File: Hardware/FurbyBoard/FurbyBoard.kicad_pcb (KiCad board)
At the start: 4 copper layers, 68.8 x 74.6 mm, 155 parts, among them J1 USB-C 16P, J11 J_EXP: header de expansión si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, J2 BAT+, J3 BAT-, J5 Micro I2S (3V3, GND, SCK, WS,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, J6 FPC 24P 0.5, J7 Frente: IR (emisor ×2, recept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, J8 Inclinación ×3, lengua ×2, al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, J9 Leva ×2, encoder ×4, barriga 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, Q1 SI7615ADN, Q2 AO3400A, Q3 AO3400A, SW1 RESET, SW2 BOOT, U1 USBLC6-2SC6, U10 TCA9535PWR, U11 SN74LVC1G17DBVR, U2 BQ24073RGTR, U3 TPS63802DLAR, U4 ESP32-S3-WROOM-1-N16R8, U5 TPS61089RNRR, U6 DRV8231ADSGR, U7 MAX98357AETE+T, U8 ME6211C28M5G-N, U9 ME6211C12M5G-N

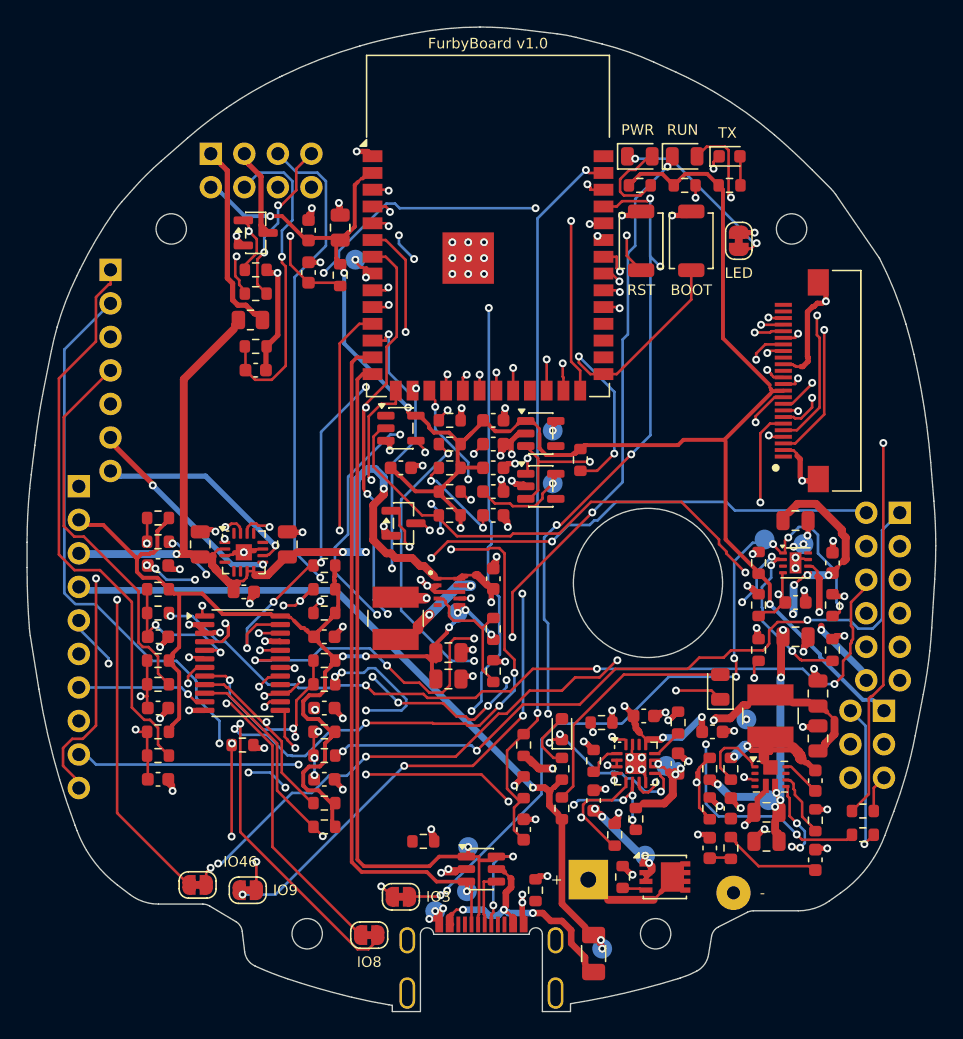
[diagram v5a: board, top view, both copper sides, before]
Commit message: Feature: replanteo de la planta y colocación de la FurbyBoard (puerta C, sin rutar)
- Partición nueva: motor y elevador en la esquina trasera derecha junto a J9, cargador en el centro trasero con los pads de batería, LDO de cámara bajo el FPC, expansor pegado a la columna izquierda del módulo, amplificador junto a J8, buck-boost en la zona trasera izquierda; J8, J5 y J_EXP en el borde izquierdo; TP en la cara inferior junto a su fuente.
- Pasillos reservados: cámara (módulo -> J6), sur, canal de la columna izquierda y norte-sur (par USB).
- gen_pcb.py: cara por pieza, keepout de cobre de las cabezas de tornillo, franja del flex sin piezas, logo recolocado; comprobar_colocacion.py vigila el flex y los TP de la cara inferior.
- Puerta C: DRC 0/0 con paridad (362 conexiones sin rutar, esperable), comprobar-flujo PASS (0 errores, 4 avisos de desacoplo a 1-1,9 mm), 12 PNG revisados. Informe en revisiones/ y NOTAS.md reescrito con la plantilla.

Co-Authored-By: Claude Fable 5.1 <noreply@anthropic.com>
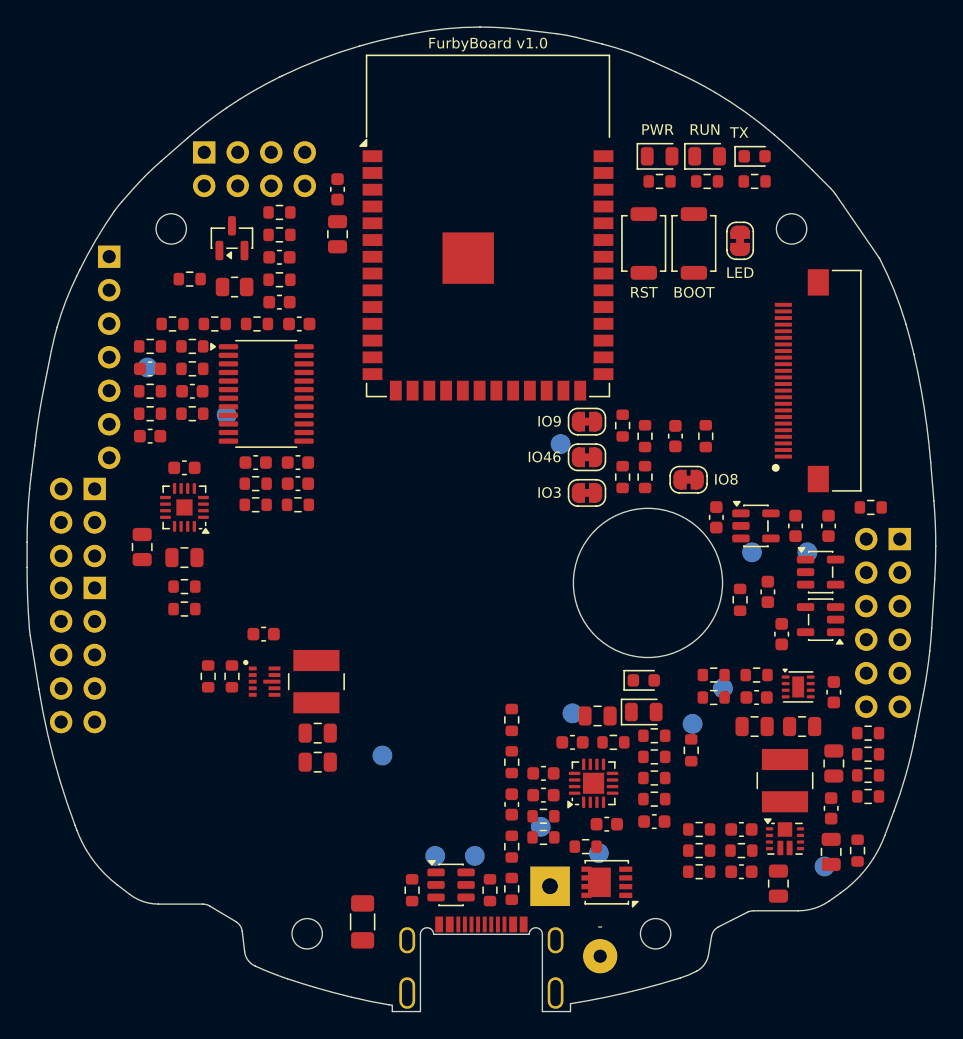
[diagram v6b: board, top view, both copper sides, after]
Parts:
- removed Q2: AO3400A, Package_TO_SOT_SMD:SOT-23
- J11: value J_EXP: header de expansión sin montar -> J_EXP: header de expansión 2 x 5 sin montar; footprint FurbyBoard:Pads_1x10_P2.54mm -> FurbyBoard:Pads_2x05_P2.54mm
- J5: value Micro I2S (3V3, GND, SCK, WS, SD, L/R) -> Micro I2S (SD, GND, SCK, WS, 3V3, GND)
- J9: value Leva ×2, encoder ×4, barriga ×2, espalda ×2, motor ×2 -> Encoder ×3, leva ×2, barriga ×2, espalda ×2, motor ×2 (más GND)
- R51: value 220 -> 470
- moved J5 62.1 mm to (117.2, 48.2)
- moved R40 55.7 mm to (175.8, 66.7)
- moved R42 54.9 mm to (175.8, 68.3)
- moved R32 54.2 mm to (124.0, 57.3)
- moved R31 54.1 mm to (124.0, 55.6)
- moved TP14 51.5 mm to (121.2, 39.0), turned to 0 degrees
- moved JP1 43.8 mm to (154.5, 43.1)
- moved JP2 43.8 mm to (154.5, 45.8)
- moved JP4 42.1 mm to (162.2, 47.5)
- moved R50 41.2 mm to (175.8, 69.9)
- moved R51 39.2 mm to (175.8, 71.5)
- moved TP12 36.6 mm to (152.5, 44.8), turned to 0 degrees
- moved U11 34.9 mm to (172.2, 58.1), turned to 180 degrees
- moved R25 34.0 mm to (162.4, 68.0), turned to 90 degrees
- moved JP3 33.7 mm to (154.5, 48.5)
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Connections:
- net BB_L1 renamed BB_SW1
- net BB_L2 renamed BB_SW2
- net MIC_SCK renamed I2S_SCK_MIC
- net MIC_WS renamed I2S_WS_MIC
- J5 pad 1: 3V3 -> I2S_DIN
- J5 pad 5: I2S_DIN -> 3V3
- J9 pad 1: HOME_PAD -> ENC_PT
- J9 pad 4: ENC_LED_K -> GND
- J9 pad 5: ENC_PT -> HOME_PAD
- R51 pad 1: 3V3 -> V6
- U10 pad 10: CHG -> PGOOD
- U10 pad 11: EXP_P07 -> CHG
- U10 pad 16: AMP_SD -> TUMMY
- U10 pad 17: CAM_PWDN -> BACK
- U10 pad 18: CAM_EN -> CAM_PWDN
- U10 pad 19: LED_RUN_K -> CAM_EN
- U10 pad 20: IR_PWR -> LED_RUN_K
- U10 pad 4: TUMMY -> TILT_A
- U10 pad 5: BACK -> TILT_B
- U10 pad 7: TILT_A -> EXP_P07
- U10 pad 8: TILT_B -> IR_PWR
- U10 pad 9: PGOOD -> AMP_SD
- U4 pad 10: HOME -> I2S_DIN
- U4 pad 11: EXP_INT -> HOME
- U4 pad 6: I2S_BCLK -> EXP_INT
- U4 pad 7: I2S_WS -> I2S_BCLK
- U4 pad 8: I2S_DOUT -> I2S_WS
- U4 pad 9: I2S_DIN -> I2S_DOUT
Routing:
- net 3V3: track 224.1 -> 0.00 mm, vias 11 -> 0
- net I2C_SCL: track 126.5 -> 0.00 mm, vias 7 -> 0
- net GND: track 112.3 -> 0.00 mm, vias 101 -> 0
- net VSYS: track 108.4 -> 0.00 mm, vias 9 -> 0
- net I2C_SDA: track 107.1 -> 0.00 mm, vias 7 -> 0
- net I2S_WS: track 95.6 -> 0.00 mm, vias 6 -> 0
- net U0TX: track 92.2 -> 0.00 mm, vias 7 -> 0
- net ENC_IO: track 90.3 -> 0.00 mm, vias 8 -> 0
- net EN_6V: track 85.3 -> 0.00 mm, vias 8 -> 0
- net TUMMY_PAD: track 81.0 -> 0.00 mm, vias 6 -> 0
- net I2S_BCLK: track 77.3 -> 0.00 mm, vias 2 -> 0
- net CAM_PWDN: track 76.8 -> 0.00 mm, vias 8 -> 0
- net VBUS: track 76.7 -> 0.00 mm, vias 6 -> 0
- net I2S_DIN: track 73.8 -> 0.00 mm, vias 1 -> 0
- net U0RX: track 71.9 -> 0.00 mm, vias 4 -> 0
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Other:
- board text added: "flex"
- board text removed: "+"
- board text removed: "1V2"
- board text removed: "2V8"
- board text removed: "5V"
- board text removed: "6V"
- board text removed: "BAR"
- board text removed: "BAT"
- board text removed: "D+"
- board text removed: "D-"
- board text removed: "EN-"
- board text removed: "ENF"
- board text removed: "I2S"
- board text removed: "IO4 SDA"
- board text removed: "IO43 TX"
- board text removed: "IO44 RX"
- board text removed: "IO5 SCL"
- board text removed: "SCK"
- board text removed: "SD"
- board text removed: "VBUS"
- board text removed: "WS"

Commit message: Feature: colocación vuelta 1 con los hallazgos R1–R9 de la revisión independiente
TP6/TP9 a ≤ 5 mm de su fuente; TPS63802 y TPS61022 con su layout de
referencia (Cin/Cout pegados, C18 a 0° bajo VOUT/GND, C14/R21 junto a
COMP/FB); RT1 bajo la batería; R23 dentro del contorno; anillo libre de
2 mm alrededor del agujero del mecanismo. Puerta C: ERC 0, DRC 0/0 con
paridad, comprobar-flujo PASS, revisar-rutado PASS; zonas revisadas en
PNG: U5, U3, U2, U6, U8, RT1, J1 y los renders de las dos caras.

Co-Authored-By: Claude Fable 5.1 <noreply@anthropic.com>
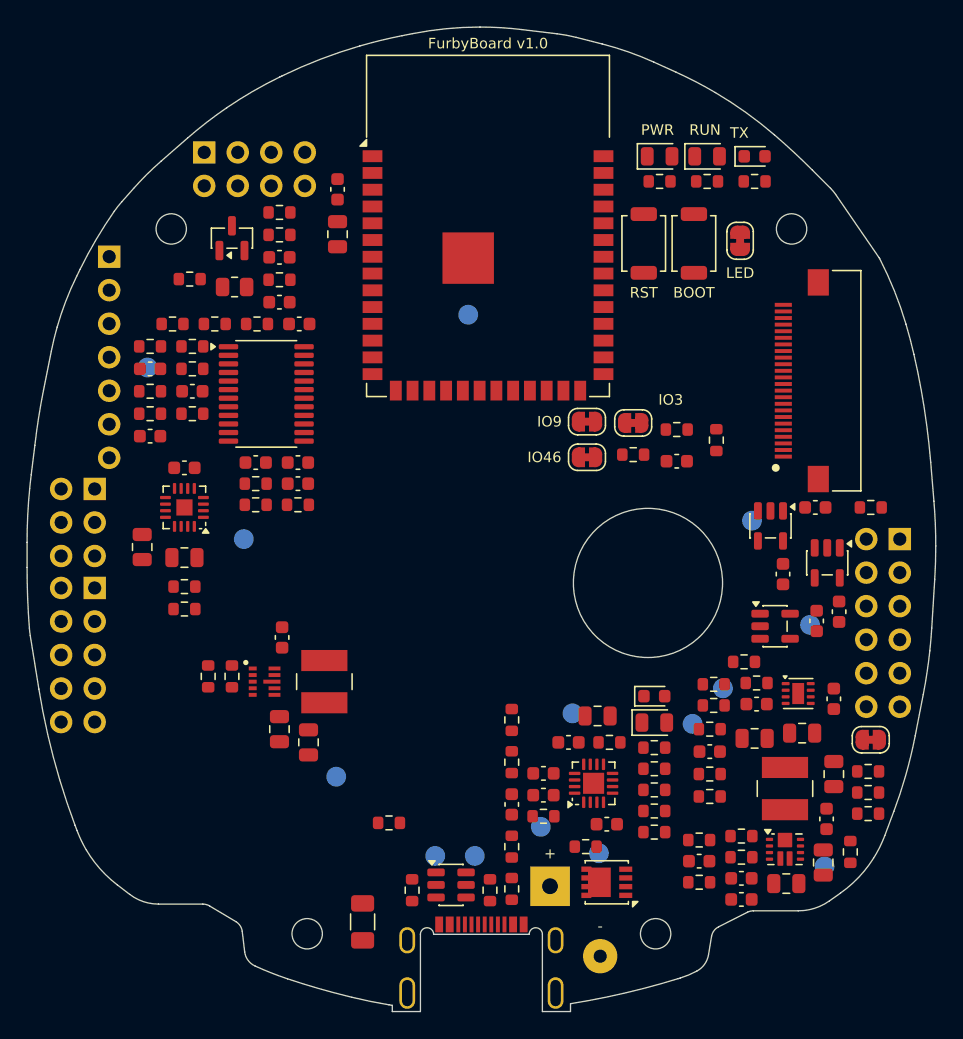
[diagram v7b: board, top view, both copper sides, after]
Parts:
- removed R3: 10k, Resistor_SMD:R_0603_1608Metric
- added RT1: 10k NTC, Resistor_SMD:R_0603_1608Metric, F.Cu at (139.5, 73.5)
- moved R34 26.1 mm to (163.8, 69.8), turned to 0 degrees
- moved R30 24.7 mm to (163.8, 71.5), turned to 0 degrees
- moved JP4 24.1 mm to (176.0, 67.2)
- moved R51 21.9 mm to (176.0, 49.6)
- moved R52 15.1 mm to (166.4, 61.3)
- moved C30 12.9 mm to (163.8, 68.1), turned to 0 degrees
- moved TP12 12.0 mm to (145.5, 35.0)
- moved R33 10.1 mm to (163.8, 66.4), turned to 0 degrees
- moved TP9 9.49 mm to (128.5, 52.0)
- moved C14 8.85 mm to (166.2, 79.3), turned to 180 degrees
- moved C27 7.54 mm to (171.8, 49.6), turned to 0 degrees
- moved R25 6.80 mm to (159.6, 74.2), turned to 0 degrees
- moved C29 6.55 mm to (173.6, 57.5), turned to -90 degrees
- moved JP3 6.35 mm to (158.0, 43.2)
- moved TP11 5.50 mm to (171.4, 58.5)
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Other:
- board text added: "+"
- board text added: "1V2"
- board text added: "2V8"
- board text added: "5V"
- board text added: "6V"
- board text added: "BAR"
- board text added: "BAT"
- board text added: "D+"
- board text added: "D-"
- board text added: "ENF"
- board text added: "I2S"
- board text added: "IO4 SDA"
- board text added: "IO43 TX"
- board text added: "IO44 RX"
- board text added: "IO5 SCL"
- board text added: "IPR"
- board text added: "SCK"
- board text added: "SD"
- board text added: "VBUS"
- board text added: "WS"
- board text removed: "EN+"
- board text removed: "ESP"

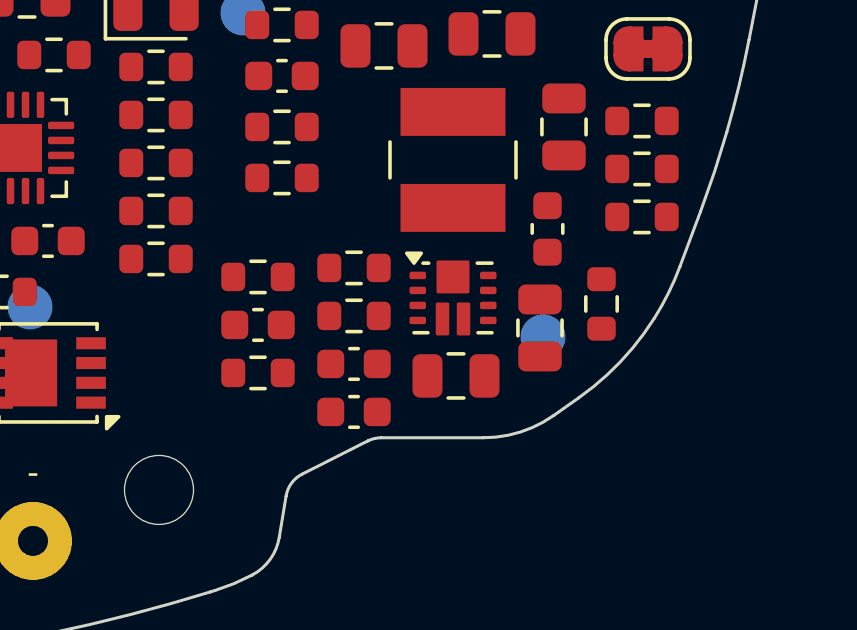
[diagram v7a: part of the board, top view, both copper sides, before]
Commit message: Fix: C12 de VCC del elevador frente a su pin (R16) y mejoras R17, R20 y R21
C12 pasa de 3,86 a 0,64 mm del pin VCC del TPS61089 intercambiándose
con R21; R24/C14 con el nodo RC de 0,65 mm; R50 y R23 con más margen
al borde; RT1 en el TEST-PLAN (V_TS, hot y cold). Ningún otro
desacoplo cambia (medido contra 96d64e1). ERC 0, DRC 0/0 con paridad,
comprobar-flujo PASS, revisar-rutado PASS; PNG de U5 y C14 revisados.

Co-Authored-By: Claude Fable 5.1 <noreply@anthropic.com>
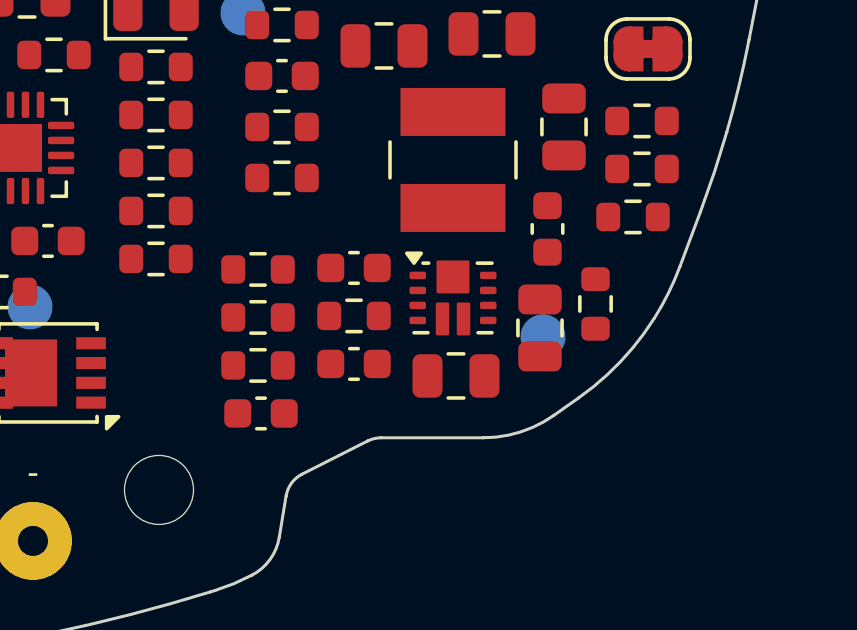
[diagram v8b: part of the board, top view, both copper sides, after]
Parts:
- moved C12 3.72 mm to (166.2, 74.5)
- moved R21 3.20 mm to (163.0, 76.2)
- moved C14 3.10 mm to (163.1, 79.3), turned to 0 degrees
- moved R22 1.60 mm to (166.2, 76.1)
- moved R50 0.30 mm to (175.5, 72.8)
- moved R20 0.25 mm to (163.0, 74.5)
- moved R24 0.25 mm to (163.0, 77.8)
- moved R23 0.20 mm to (174.2, 75.7)
